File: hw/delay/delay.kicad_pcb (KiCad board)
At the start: 2 copper layers, 38.4 x 58.9 mm, 24 parts, among them J1 conn_trigger, J2 conn_done, J3 FTDI, J4 conn_active, SW1 Rotary_Encoder_Switch, SW2 switch_active, SW3 switch_reset, U1 ATmega328P-PU, U2 LTC-4724JR, Y1 Crystal

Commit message: DELAY block v2
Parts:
- removed J2: conn_done, Connector_PinHeader_2.54mm:PinHeader_1x03_P2.54mm_Vertical
- removed J4: conn_active, Connector_PinHeader_2.54mm:PinHeader_1x03_P2.54mm_Vertical
- added D2: DIODE, Diode_SMD:D_0603_1608Metric, F.Cu at (133.5, 122.4)
- added H5: led_spy_hole, MountingHole:MountingHole_3.2mm_M3, F.Cu at (151.6, 105.9)
- added J5: BUS, Connector_PinHeader_2.54mm:PinHeader_2x07_P2.54mm_Vertical, F.Cu at (149.1, 95.0)
- added R5: 1k, Resistor_SMD:R_0603_1608Metric, F.Cu at (137.4, 122.5)
- added R6: 1k, Resistor_SMD:R_0603_1608Metric, F.Cu at (141.3, 122.4)
- added R7: 1k, Resistor_SMD:R_0603_1608Metric, F.Cu at (146.5, 123.5)
- added SW4: NEXT, Package_DIP:DIP-16_W7.62mm_SMDSocket_SmallPads, F.Cu at (136.4, 141.7)
- added SW5: ACTIVE, Package_DIP:DIP-16_W7.62mm_SMDSocket_SmallPads, F.Cu at (136.4, 130.3)
- added SW6: ID, Package_DIP:DIP-16_W7.62mm_SMDSocket_SmallPads, F.Cu at (136.4, 153.2)
- C1: footprint Capacitor_THT:CP_Radial_Tantal_D6.0mm_P2.50mm -> Capacitor_SMD:C_0603_1608Metric
- C2, C3: footprint Capacitor_THT:C_Disc_D3.0mm_W1.6mm_P2.50mm -> Capacitor_SMD:C_0603_1608Metric
- C4, C5: footprint Capacitor_THT:C_Axial_L5.1mm_D3.1mm_P7.50mm_Horizontal -> Capacitor_SMD:C_0603_1608Metric
- D1, SW1, U2: moved to B.Cu
- H1, H2, H3, H4: footprint MountingHole:MountingHole_2.2mm_M2 -> MountingHole:MountingHole_3.2mm_M3_Pad
- J1: value conn_trigger -> bootloader; footprint Connector_PinHeader_2.54mm:PinHeader_1x03_P2.54mm_Vertical -> autoblocks:edge_connector_3
- J3: footprint Connector_PinHeader_2.54mm:PinHeader_1x06_P2.54mm_Vertical -> autoblocks:edge_connector_3
- R1, R2, R3, R4: footprint Resistor_THT:R_Axial_DIN0207_L6.3mm_D2.5mm_P10.16mm_Horizontal -> Resistor_SMD:R_0603_1608Metric
- SW2: value switch_active -> active; footprint autoblocks:SW_PUSH_6mm_H5mm -> Button_Switch_SMD:SW_SPST_TL3305C
- SW3: value switch_reset -> reset; footprint autoblocks:SW_PUSH_6mm_H5mm -> Button_Switch_SMD:SW_SPST_TL3305C
- U1: value ATmega328P-PU -> ATmega328-AU; footprint Package_DIP:DIP-28_W7.62mm -> Package_QFP:TQFP-32_7x7mm_P0.8mm
- Y1: footprint Crystal:Crystal_HC18-U_Vertical -> Crystal:Crystal_SMD_HC49-SD
- moved H2 55.2 mm to (128.0, 166.6)
- moved H1 53.5 mm to (154.7, 166.6)
- moved C3 45.3 mm to (146.5, 121.4)
- moved D1 42.0 mm to (150.1, 103.2)
- moved C2 40.9 mm to (146.3, 119.4), turned to 0 degrees
- moved SW1 40.2 mm to (138.2, 153.2), turned to 270 degrees
- moved Y1 37.0 mm to (152.4, 117.8), turned to 270 degrees
- moved R1 35.2 mm to (141.0, 106.9), turned to 0 degrees
- moved SW2 33.2 mm to (145.8, 104.4), turned to 90 degrees
- moved U2 31.9 mm to (143.3, 134.1)
- moved C5 30.5 mm to (136.9, 103.1), turned to 0 degrees
- moved H3 29.5 mm to (154.7, 96.8)
- moved C4 25.8 mm to (136.9, 106.9), turned to 180 degrees
- moved R2 24.7 mm to (133.1, 106.8), turned to 180 degrees
- moved U1 24.6 mm to (137.7, 114.7)
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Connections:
- C1 pad 1: VCC -> bus11
- C1 pad 2: GND -> bus13
- C2 pad 1: GND -> bus13
- C3 pad 1: GND -> bus13
- C4 pad 2: GND -> bus13
- D1 pad 1: GND -> bus13
- H1 pad 1: GND -> Net-(H1-Pad1)
- H2 pad 1: GND -> Net-(H2-Pad1)
- H3 pad 1: GND -> Net-(H3-Pad1)
- H4 pad 1: GND -> Net-(H4-Pad1)
- J1 pad 1: a0 -> bus13
- J1 pad 2: GND -> bus11
- J1 pad 3: VCC -> d10
- J3 pad 1: GND -> bus13
- J3 pad 2: GND -> bus13
- J3 pad 3: VCC -> bus11
- R2 pad 1: VCC -> bus11
- R3 pad 2: VCC -> bus11
- R4 pad 2: VCC -> bus11
- SW1 pad C: GND -> bus13
- SW1 pad S2: GND -> bus13
- SW2 pad 2: GND -> bus13
- SW3 pad 1: GND -> bus13
- U1 pad 1: RESET -> d3
- U1 pad 10: XTAL2 -> d6
- U1 pad 11: d5 -> d7
- U1 pad 12: d6 -> d8
- U1 pad 13: d7 -> d9
- U1 pad 14: d8 -> d10
- U1 pad 15: d9 -> d11
- U1 pad 16: d10 -> d12
- U1 pad 17: d11 -> d13
- U1 pad 18: d12 -> bus11
- U1 pad 19: d13 -> Net-(U1-Pad19)
- U1 pad 2: RX -> d4
- U1 pad 20: VCC -> AREF
- U1 pad 21: AREF -> bus13
- U1 pad 22: GND -> Net-(U1-Pad22)
- U1 pad 3: TX -> bus13
- U1 pad 4: d2 -> bus11
- U1 pad 5: d3 -> bus13
- U1 pad 6: d4 -> bus11
- U1 pad 7: VCC -> XTAL1
- U1 pad 8: GND -> XTAL2
- U1 pad 9: XTAL1 -> d5
- U2 pad 1: d13 -> Net-(R5-Pad2)
- U2 pad 5: a4 -> Net-(R6-Pad2)
- U2 pad 7: a5 -> Net-(R7-Pad2)
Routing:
- net GND: track 189.2 -> 0.00 mm
- net VCC: track 156.8 -> 0.00 mm
- net bus11: track 0.00 -> 132.4 mm, vias 0 -> 7
- net d12: track 22.3 -> 143.6 mm, vias 0 -> 2
- net bus13: track 0.00 -> 113.1 mm, vias 0 -> 4
- net d10: track 55.2 -> 146.6 mm
- net d11: track 38.7 -> 128.9 mm, vias 0 -> 1
- net bus2: track 0.00 -> 70.2 mm, vias 0 -> 1
- net bus6: track 0.00 -> 69.8 mm, vias 0 -> 1
- net bus3: track 0.00 -> 64.3 mm, vias 0 -> 1
- net bus5: track 0.00 -> 63.8 mm, vias 0 -> 1
- net bus4: track 0.00 -> 62.4 mm, vias 0 -> 1
- net bus1: track 0.00 -> 62.1 mm, vias 0 -> 1
- net bus7: track 0.00 -> 61.6 mm, vias 0 -> 1
- net bus8: track 0.00 -> 59.0 mm, vias 0 -> 1
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- added copper zone on B.Cu, net bus11
- added copper zone on F.Cu, net bus13
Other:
- board size 38.4 x 58.9 mm -> 34.3 x 77.5 mm
- rule trace_min: 0.2 -> 0.16
- board text added: "BOOT"
- board text added: "FTDI"
- board text added: "First"
- board text added: "ID"
- board text added: "NEXT"
- board text added: "Next"
- board text added: "v2"
- board text removed: "IN"
- board text removed: "RTS"
- board text removed: "v1"

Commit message: update
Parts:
- moved H5 0.16 mm to (151.6, 106.1)
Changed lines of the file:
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@@
   )
   (setup
-    (last_trace_width 0.16)
+    (last_trace_width 0.25)
     (user_trace_width 0.16)
     (user_trace_width 1)
@@
   )
   (module MountingHole:MountingHole_3.2mm_M3 (layer F.Cu)
-    (at 151.5655 105.918)
+    (at 151.575 106.075)
     (descr "Mounting Hole 3.2mm, no annular, M3")
     (tags "mounting hole 3.2mm no annular m3")
@@
     (effects (font (size 4 3.85) (thickness 0.3)) (justify mirror))
   )
-  (via (at 134.29 122.428) (size 0.8) (drill 0.4) (layers F.Cu B.Cu) (net 11))
-  (via (at 137.668 103.124) (size 0.8) (drill 0.4) (layers F.Cu B.Cu) (net 5))
-  (via (at 127.508 126.492) (size 0.8) (drill 0.4) (layers F.Cu B.Cu) (net 9))
-  (via (at 132.588 134.112) (size 0.8) (drill 0.4) (layers F.Cu B.Cu) (net 29))
-  (via (at 142.748 134.112) (size 0.8) (drill 0.4) (layers F.Cu B.Cu) (net 29))
-  (via (at 140.208 134.112) (size 0.8) (drill 0.4) (layers F.Cu B.Cu) (net 29))
-  (via (at 137.668 134.112) (size 0.8) (drill 0.4) (layers F.Cu B.Cu) (net 29))
-  (via (at 135.128 134.112) (size 0.8) (drill 0.4) (layers F.Cu B.Cu) (net 29))
-  (via (at 130.048 134.112) (size 0.8) (drill 0.4) (layers F.Cu B.Cu) (net 29))
-  (via (at 127.508 134.112) (size 0.8) (drill 0.4) (layers F.Cu B.Cu) (net 29))
-  (via (at 145.288 145.542) (size 0.8) (drill 0.4) (layers F.Cu B.Cu) (net 8))
-  (via (at 142.748 145.542) (size 0.8) (drill 0.4) (layers F.Cu B.Cu) (net 8))
-  (via (at 140.208 145.542) (size 0.8) (drill 0.4) (layers F.Cu B.Cu) (net 8))
-  (via (at 137.668 145.542) (size 0.8) (drill 0.4) (layers F.Cu B.Cu) (net 8))
-  (via (at 135.128 145.542) (size 0.8) (drill 0.4) (layers F.Cu B.Cu) (net 8))
-  (via (at 132.588 145.542) (size 0.8) (drill 0.4) (layers F.Cu B.Cu) (net 8))
-  (via (at 130.048 145.542) (size 0.8) (drill 0.4) (layers F.Cu B.Cu) (net 8))
   (segment (start 147.6525 119.448) (end 147.115 119.448) (width 0.16) (layer F.Cu) (net 1))
   (segment (start 148.502 119.448) (end 147.6525 119.448) (width 0.16) (layer F.Cu) (net 1))
@@
   (segment (start 131.688456 110.688456) (end 131.688456 109.367915) (width 0.16) (layer F.Cu) (net 4))
   (segment (start 133.46 115.11) (end 132.5 115.11) (width 0.16) (layer F.Cu) (net 4))
+  (via (at 137.668 103.124) (size 0.8) (drill 0.4) (layers F.Cu B.Cu) (net 5))
   (segment (start 129.54 100.584) (end 124.58601 105.53799) (width 0.16) (layer B.Cu) (net 5))
   (segment (start 125.222 113.284) (end 127.762 113.284) (width 0.16) (layer B.Cu) (net 5))
@@
   (segment (start 130.919998 116.826402) (end 130.919998 116.073598) (width 0.16) (layer F.Cu) (net 7))
   (segment (start 132.1 119.859536) (end 132.1 118.006404) (width 0.16) (layer F.Cu) (net 7))
+  (via (at 145.288 145.542) (size 0.8) (drill 0.4) (layers F.Cu B.Cu) (net 8))
+  (via (at 142.748 145.542) (size 0.8) (drill 0.4) (layers F.Cu B.Cu) (net 8))
+  (via (at 140.208 145.542) (size 0.8) (drill 0.4) (layers F.Cu B.Cu) (net 8))
+  (via (at 137.668 145.542) (size 0.8) (drill 0.4) (layers F.Cu B.Cu) (net 8))
+  (via (at 135.128 145.542) (size 0.8) (drill 0.4) (layers F.Cu B.Cu) (net 8))
+  (via (at 132.588 145.542) (size 0.8) (drill 0.4) (layers F.Cu B.Cu) (net 8))
+  (via (at 130.048 145.542) (size 0.8) (drill 0.4) (layers F.Cu B.Cu) (net 8))
   (segment (start 127.508 145.542) (end 127.508 145.542) (width 0.16) (layer F.Cu) (net 8))
   (segment (start 127.708812 145.542) (end 127.608406 145.441594) (width 0.16) (layer B.Cu) (net 8))
@@
   (segment (start 130.048 138.938) (end 126.385989 135.275989) (width 0.16) (layer B.Cu) (net 8))
   (segment (start 130.451122 124.56601) (end 132.458823 122.558309) (width 0.16) (layer B.Cu) (net 8))
+  (via (at 127.508 126.492) (size 0.8) (drill 0.4) (layers F.Cu B.Cu) (net 9))
   (segment (start 135.89 108.966) (end 135.89 107.671988) (width 0.16) (layer B.Cu) (net 9))
   (via (at 134.574252 115.923872) (size 0.8) (drill 0.4) (layers F.Cu B.Cu) (net 9))
@@
   (segment (start 131.809998 116.71) (end 131.6 116.500002) (width 0.16) (layer F.Cu) (net 10))
   (via (at 131.6 116.500002) (size 0.8) (drill 0.4) (layers F.Cu B.Cu) (net 10))
+  (via (at 134.29 122.428) (size 0.8) (drill 0.4) (layers F.Cu B.Cu) (net 11))
   (via (at 141.666 106.934) (size 0.8) (drill 0.4) (layers F.Cu B.Cu) (net 11))
   (via (at 138.650325 113.722005) (size 0.8) (drill 0.4) (layers F.Cu B.Cu) (net 11))
@@
   (segment (start 142.062 113.408) (end 141.96 113.51) (width 0.16) (layer F.Cu) (net 13))
   (segment (start 145.455 113.408) (end 145.542 113.538) (width 0.16) (layer F.Cu) (net 13))
-  (segment (start 144.296 106.944) (end 144.296 100.794) (width 0.25) (layer F.Cu) (net 15))
-  (segment (start 144.296 107.994) (end 144.296 107.994) (width 0.25) (layer F.Cu) (net 15))
-  (segment (start 147.03 115.4105) (end 147.0675 115.448) (width 0.16) (layer F.Cu) (net 27))
-  (segment (start 147.03 113.408) (end 147.03 115.4105) (width 0.16) (layer F.Cu) (net 27))
-  (segment (start 137.31 108.1) (end 136.144 106.934) (width 0.16) (layer F.Cu) (net 28))
-  (segment (start 137.31 110.46) (end 137.31 108.1) (width 0.16) (layer F.Cu) (net 28))
   (segment (start 126.516 117.602) (end 128.016 117.602) (width 0.16) (layer F.Cu) (net 13))
   (segment (start 145.542 113.538) (end 142.062 113.408) (width 0.16) (layer F.Cu) (net 13))
@@
   (segment (start 141.912 167.662) (end 140.971132 166.721132) (width 0.16) (layer B.Cu) (net 14))
   (segment (start 143.176 167.662) (end 141.912 167.662) (width 0.16) (layer B.Cu) (net 14))
+  (segment (start 144.296 106.944) (end 144.296 100.794) (width 0.25) (layer F.Cu) (net 15))
+  (segment (start 144.296 107.994) (end 144.296 107.994) (width 0.25) (layer F.Cu) (net 15))
   (segment (start 144.296 107.994) (end 144.296 106.944) (width 0.25) (layer F.Cu) (net 15))
   (via (at 144.296 107.994) (size 0.8) (drill 0.4) (layers F.Cu B.Cu) (net 15))
@@
   (segment (start 135.636 122.174) (end 135.636 123.19) (width 0.16) (layer F.Cu) (net 26))
   (segment (start 135.636 123.19) (end 134.62 124.206) (width 0.16) (layer F.Cu) (net 26))
+  (segment (start 147.03 115.4105) (end 147.0675 115.448) (width 0.16) (layer F.Cu) (net 27))
+  (segment (start 147.03 113.408) (end 147.03 115.4105) (width 0.16) (layer F.Cu) (net 27))
   (via (at 133.905 106.83) (size 0.8) (drill 0.4) (layers F.Cu B.Cu) (net 27))
   (segment (start 128.246 113.284) (end 126.746 113.284) (width 0.16) (layer F.Cu) (net 27))
@@
   (segment (start 129.820001 131.344001) (end 141.216161 131.344001) (width 0.16) (layer B.Cu) (net 27))
   (segment (start 139.210834 120.89461) (end 139.210834 120.328925) (width 0.16) (layer B.Cu) (net 27))
+  (segment (start 137.31 108.1) (end 136.144 106.934) (width 0.16) (layer F.Cu) (net 28))
+  (segment (start 137.31 110.46) (end 137.31 108.1) (width 0.16) (layer F.Cu) (net 28))
   (segment (start 126.492 107.95) (end 126.746 108.204) (width 0.16) (layer F.Cu) (net 28))
   (segment (start 126.746 110.744) (end 126.746 108.204) (width 0.16) (layer F.Cu) (net 28))
@@
   (segment (start 129.262 110.744) (end 130.736354 112.218354) (width 0.16) (layer F.Cu) (net 28))
   (segment (start 126.534313 115.500016) (end 127.2479 114.786429) (width 0.16) (layer B.Cu) (net 28))
+  (via (at 132.588 134.112) (size 0.8) (drill 0.4) (layers F.Cu B.Cu) (net 29))
+  (via (at 142.748 134.112) (size 0.8) (drill 0.4) (layers F.Cu B.Cu) (net 29))
+  (via (at 140.208 134.112) (size 0.8) (drill 0.4) (layers F.Cu B.Cu) (net 29))
+  (via (at 137.668 134.112) (size 0.8) (drill 0.4) (layers F.Cu B.Cu) (net 29))
+  (via (at 135.128 134.112) (size 0.8) (drill 0.4) (layers F.Cu B.Cu) (net 29))
+  (via (at 130.048 134.112) (size 0.8) (drill 0.4) (layers F.Cu B.Cu) (net 29))
+  (via (at 127.508 134.112) (size 0.8) (drill 0.4) (layers F.Cu B.Cu) (net 29))
   (via (at 145.288 134.112) (size 0.8) (drill 0.4) (layers F.Cu B.Cu) (net 29))
   (segment (start 145.288 134.112) (end 127.508 134.112) (width 0.16) (layer B.Cu) (net 29))

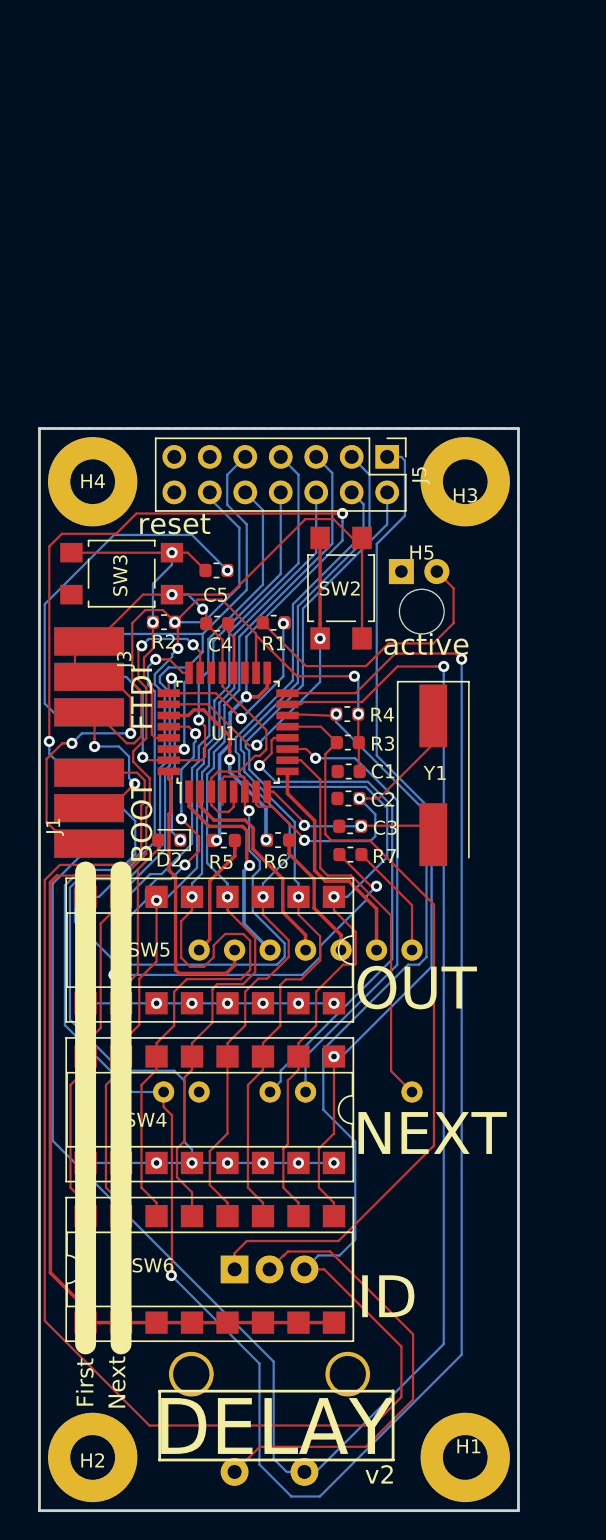
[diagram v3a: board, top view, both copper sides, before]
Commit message: fix DELAY bus assigments
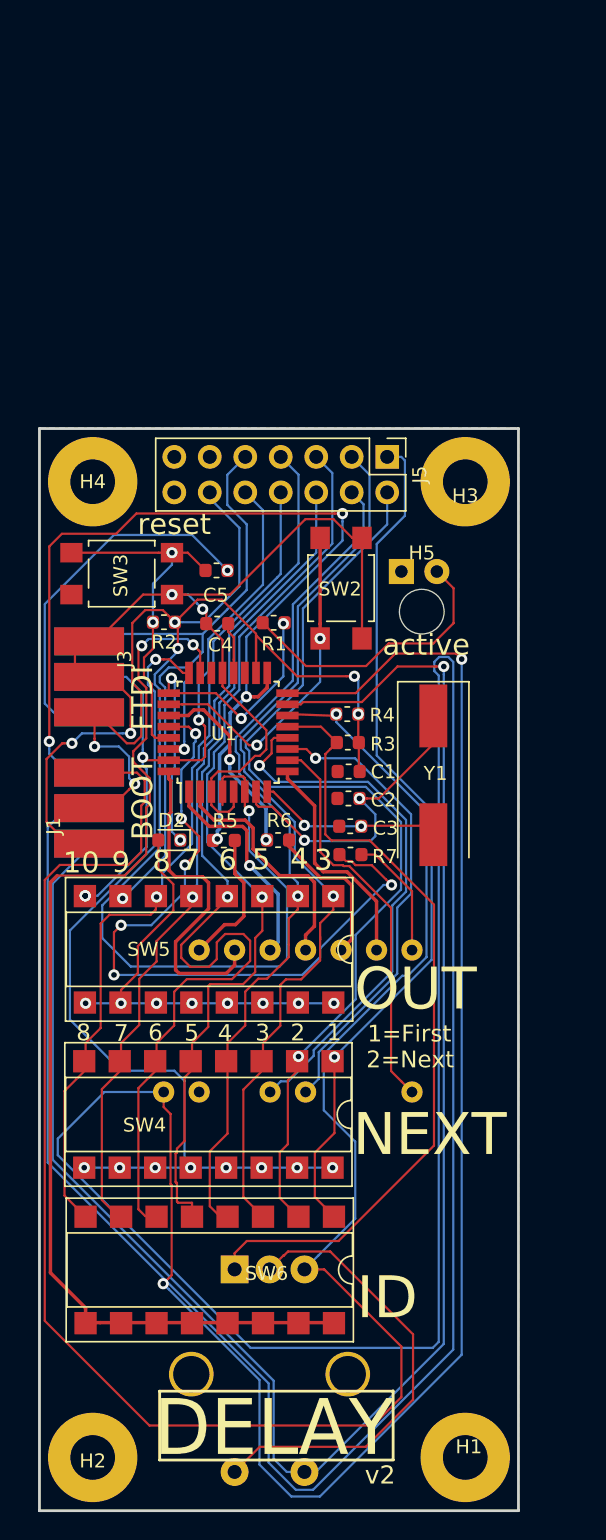
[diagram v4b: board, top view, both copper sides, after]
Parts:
- moved SW4 0.35 mm to (136.3, 142.1)
- moved SW5 0.07 mm to (136.3, 130.2)
- turned SW6 to 270 degrees
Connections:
- SW5 pad 1: bus2 -> bus3
- SW5 pad 2: bus3 -> bus4
- SW5 pad 3: bus4 -> bus5
- SW5 pad 4: bus5 -> bus6
- SW5 pad 5: bus6 -> bus7
- SW5 pad 6: bus7 -> bus8
- SW5 pad 7: bus8 -> RX
- SW5 pad 8: RX -> TX
- SW6 pad 1: a0 -> bus1
- SW6 pad 10: bus2 -> a0
- SW6 pad 11: bus3 -> a0
- SW6 pad 12: bus4 -> a0
- SW6 pad 13: bus5 -> a0
- SW6 pad 14: bus6 -> a0
- SW6 pad 15: bus7 -> a0
- SW6 pad 16: bus8 -> a0
- SW6 pad 2: a0 -> bus2
- SW6 pad 3: a0 -> bus3
- SW6 pad 4: a0 -> bus4
- SW6 pad 5: a0 -> bus5
- SW6 pad 6: a0 -> bus6
- SW6 pad 7: a0 -> bus7
- SW6 pad 8: a0 -> bus8
- SW6 pad 9: bus1 -> a0
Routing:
- net d12: track 143.6 -> 330.2 mm
- net TX: track 36.1 -> 48.5 mm, vias 2 -> 4
- net bus11: track 132.4 -> 128.3 mm
- net d2: track 20.2 -> 23.3 mm
- net RX: track 56.7 -> 54.1 mm
- net a5: track 49.1 -> 51.7 mm
- net bus6: track 69.8 -> 71.8 mm
- net bus8: track 59.0 -> 60.9 mm
- net d4: track 15.8 -> 17.5 mm
- net Net-(R6-Pad2): track 9.58 -> 11.2 mm
- net bus5: track 63.8 -> 65.3 mm
- net bus3: track 64.3 -> 65.6 mm
- net a1: track 67.0 -> 65.7 mm
- net bus2: track 70.2 -> 68.9 mm
- net d10: track 146.6 -> 145.5 mm
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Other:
- board text added: "1"
- board text added: "10"
- board text added: "1=First"
- board text added: "2"
- board text added: "2=Next"
- board text added: "3"
- board text added: "4"
- board text added: "5"
- board text added: "6"
- board text added: "7"
- board text added: "8"
- board text added: "9"
- board text removed: "First"
- board text removed: "Next"
